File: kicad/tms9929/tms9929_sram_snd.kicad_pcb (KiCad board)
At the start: 2 copper layers, 160 x 100.3 mm, 66 parts, among them P1 CONN_01X03, P4 Power, P5 CONN_02X25, Q1 BC550, Q10 BC550, Q2 BC550, Q3 BC550, Q4 BC550, Q5 BC550, Q6 BC550, Q7 BC550, Q8 BC550, Q9 BC550, U1 TMS9929A, U10 7400, U2 74HCT04, U3 74HCT574, U4 74HCT574, U5 74HCT574, U6 HM62256BLFP-5SLT

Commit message: +update
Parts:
- RV1, RV2, RV3: footprint w_pth_resistors:trimmer_piher_pt15xvx2 -> Potentiometers:Potentiometer_Trimmer-Piher_PT15-V15_horizontal
- moved P1 102.1 mm to (130.8, 54.6), turned to 90 degrees
- moved R17 55.9 mm to (100.3, 133.3)
- moved R21 55.9 mm to (100.3, 129.5)
- moved Q7 55.9 mm to (100.3, 137.2)
- moved Q6 55.9 mm to (108.0, 137.2)
- moved C14 54.7 mm to (109.2, 130.8)
- moved RV2 52.3 mm to (95.2, 58.4), turned to 270 degrees
- moved RV3 51.8 mm to (95.2, 114.3), turned to 270 degrees
- moved C16 44.5 mm to (109.2, 74.9)
- moved R19 43.3 mm to (100.3, 77.5)
- moved R23 43.3 mm to (100.3, 73.7)
- moved Q9 43.2 mm to (100.3, 81.3)
- moved Q5 43.2 mm to (108.0, 81.3)
- moved Q3 31.9 mm to (120.7, 78.7)
- moved R11 31.9 mm to (120.7, 90.2), turned to 0 degrees
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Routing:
- net GND: track 262.2 -> 741.6 mm, vias 0 -> 1
- net VCC: track 47.2 -> 254.5 mm, vias 0 -> 1
- net /12VS: track 31.7 -> 180.7 mm
- net Net-(C14-Pad2): track 19.7 -> 67.8 mm
- net Net-(Q2-Pad3): track 60.3 -> 13.6 mm
- net /RGB-G: track 0.00 -> 44.1 mm
- net /R-Y: track 57.5 -> 99.6 mm
- net Net-(Q3-Pad3): track 49.8 -> 14.9 mm
- net Net-(Q1-Pad3): track 47.0 -> 78.1 mm
- net Net-(Q9-Pad2): track 0.00 -> 22.4 mm
- net Net-(Q4-Pad3): track 3.81 -> 26.1 mm
- net Net-(Q7-Pad2): track 0.00 -> 21.3 mm
- net Net-(Q8-Pad2): track 0.00 -> 21.3 mm
- net /RGB-R: track 0.00 -> 19.9 mm
- net /RGB-B: track 0.00 -> 19.6 mm
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
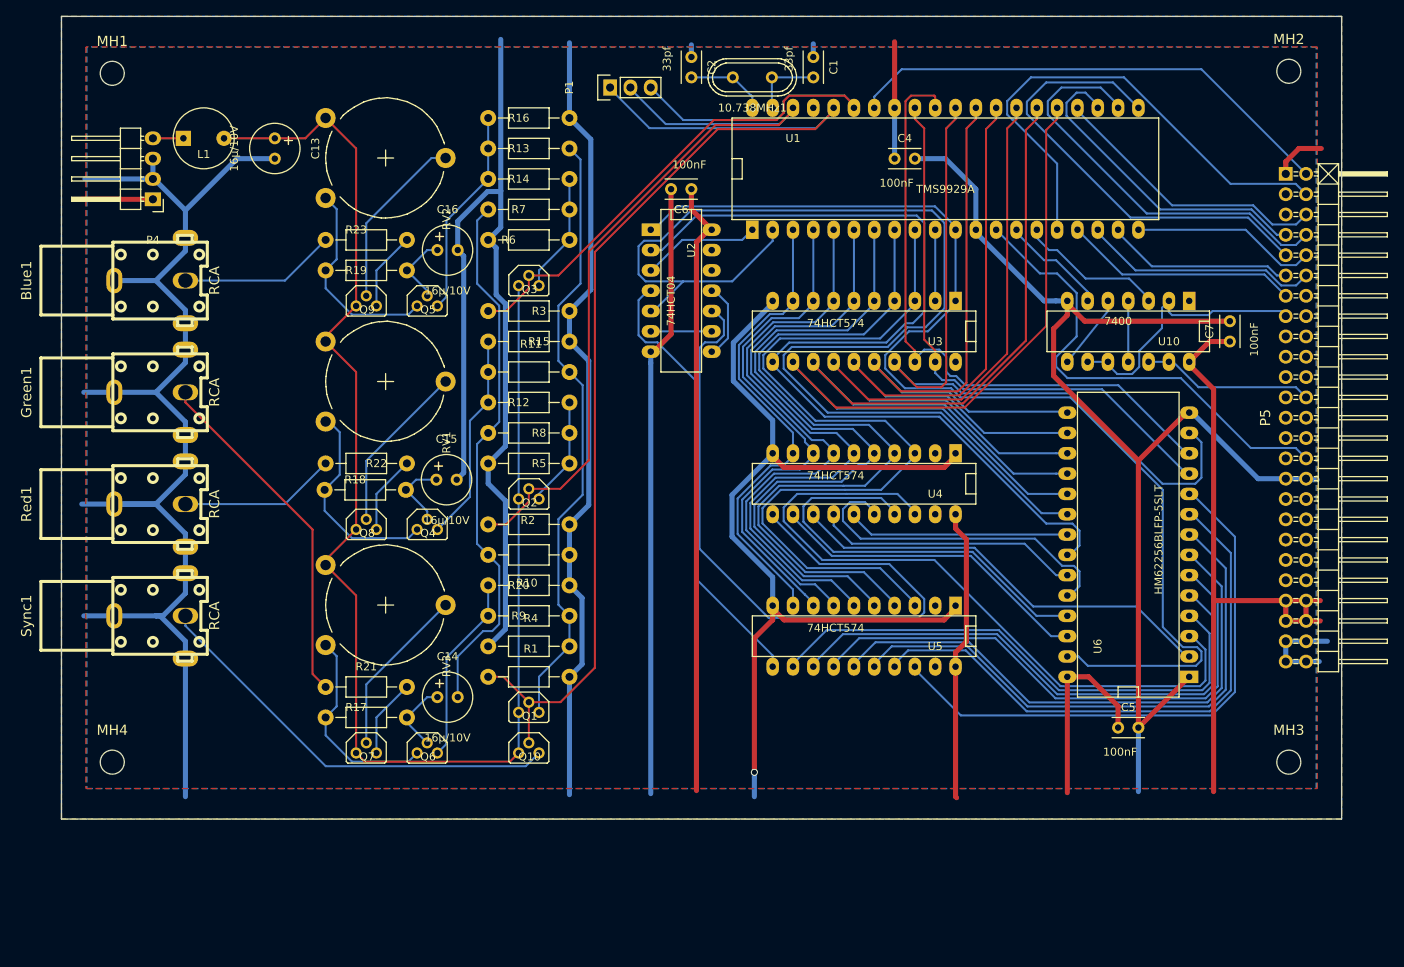
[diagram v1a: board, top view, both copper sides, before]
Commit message: +before gnd area
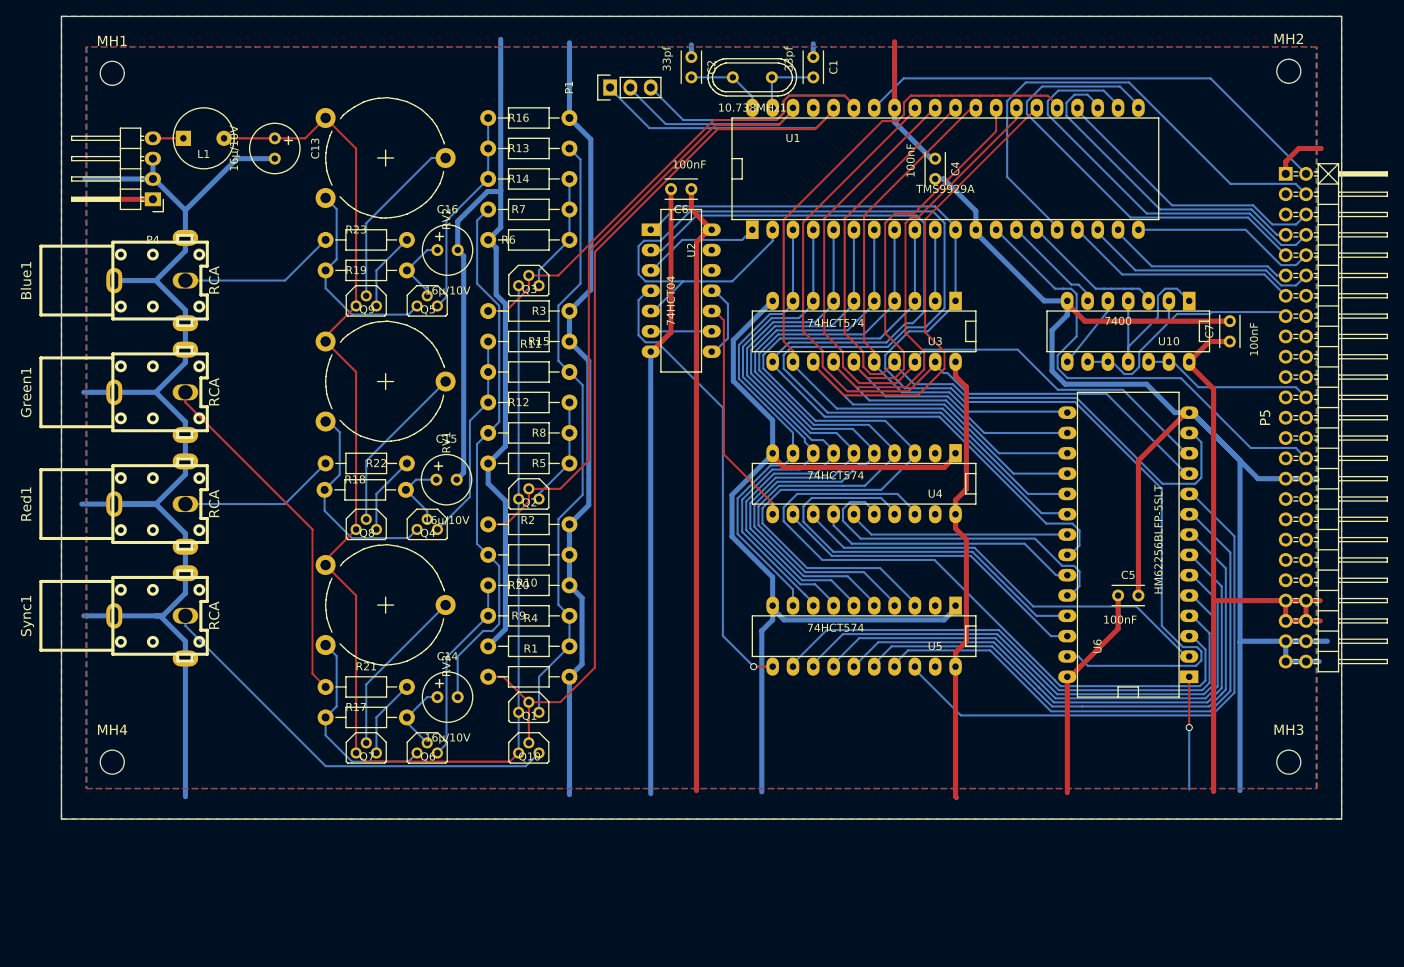
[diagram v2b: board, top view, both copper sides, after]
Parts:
- moved C5 16.5 mm to (194.3, 118.1)
- moved C4 5.08 mm to (171.4, 63.5), turned to 270 degrees
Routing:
- net /COL: track 89.9 -> 29.5 mm
- net GND: track 741.6 -> 775.4 mm
- net VCC: track 254.5 -> 279.5 mm
- net /RD0: track 71.5 -> 94.4 mm
- net Net-(U10-Pad1): track 10.5 -> 25.2 mm
- net /RD1: track 81.5 -> 92.2 mm
- net /RD3: track 75.8 -> 65.6 mm
- net /RD7: track 108.3 -> 102.6 mm
- net /RD4: track 83.9 -> 79.1 mm
- net /RD5: track 91.6 -> 87.8 mm
- net /RD6: track 99.6 -> 96.9 mm
- net /RW: track 35.8 -> 33.9 mm
- net /ROW: track 56.0 -> 57.8 mm, vias 0 -> 1
- net /RESET: track 62.2 -> 60.4 mm
- net /RD2: track 95.4 -> 96.8 mm
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
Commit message: +update
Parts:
- moved R1 5.08 mm to (125.7, 128.3)
- moved R2 5.08 mm to (125.7, 109.2)
- moved R3 5.08 mm to (125.7, 82.5)
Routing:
- net /12VS: track 180.7 -> 228.6 mm
- net GND: track 775.4 -> 790.7 mm
- net /B-Y: track 89.9 -> 86.5 mm
- net /R-Y: track 99.6 -> 96.2 mm
- net /Y: track 142.6 -> 139.4 mm

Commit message: +update
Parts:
- moved Q1 3.81 mm to (120.7, 128.3)
- moved R1 3.81 mm to (125.7, 132.1)
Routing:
- net GND: track 790.7 -> 812.0 mm
- net Net-(Q1-Pad3): track 78.1 -> 74.3 mm
- net /Y: track 139.4 -> 136.2 mm
- net /SYNC: track 54.0 -> 54.6 mm
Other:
- board text added: "Steckschwein VDP/Video Board 2015 Thomas Woinke / Marko Lauke http://www.steckschwein.de/"

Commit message: +proposed final - before filled zones
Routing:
- net GND: track 812.0 -> 817.5 mm

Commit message: +final 2
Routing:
- net GND: track 817.5 -> 803.9 mm
- net /SYNC: track 54.6 -> 53.2 mm

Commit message: +final 3 - no drc errors
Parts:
- added C3: 100nF, Capacitors_ThroughHole:C_Disc_D3_P2.5, F.Cu at (179.1, 105.4)
- added C8: 100nF, Capacitors_ThroughHole:C_Disc_D3_P2.5, F.Cu at (179.1, 124.5)
- added C9: 100nF, Capacitors_ThroughHole:C_Disc_D3_P2.5, F.Cu at (179.1, 86.4)
- added G***: LOGO, qrcode:QRCODE, F.Cu at (81.3, 135.9)
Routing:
- net GND: track 803.9 -> 866.1 mm
- net VCC: track 279.5 -> 294.3 mm
- net /A7: track 88.4 -> 90.9 mm
- net /WR: track 121.5 -> 122.7 mm
- net (no net): track 0.71 -> 0.00 mm
- net /RW: track 33.9 -> 34.5 mm

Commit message: +final 4 - labels, impr. gnd
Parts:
- moved P1 9.25 mm to (133.3, 63.5), turned to 180 degrees
- renumbered 10.738MHz1 to 10.738MHz
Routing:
- net /Y: track 135.9 -> 109.2 mm
- net /B-Y: track 86.1 -> 61.3 mm
- net /R-Y: track 96.3 -> 78.3 mm
- net Net-(U10-Pad1): track 25.2 -> 19.3 mm
- net /RW: track 34.5 -> 36.0 mm
- net /WR: track 122.7 -> 121.2 mm
- net /50Pin/A0: track 59.4 -> 58.2 mm
- net GND: track 866.1 -> 865.4 mm
- net Net-(U1-Pad14): track 13.1 -> 12.6 mm
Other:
- board text added: "Bottom-Layer"
- board text added: "Top-Layer"
